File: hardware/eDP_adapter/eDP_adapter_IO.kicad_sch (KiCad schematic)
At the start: 15 parts, among them J1 DF12NB(3.0)-30DS-0.5V(51), J2 DF12NB(3.0)-30DS-0.5V(51), J3 Conn_01x30, J5 Conn_01x06_Socket

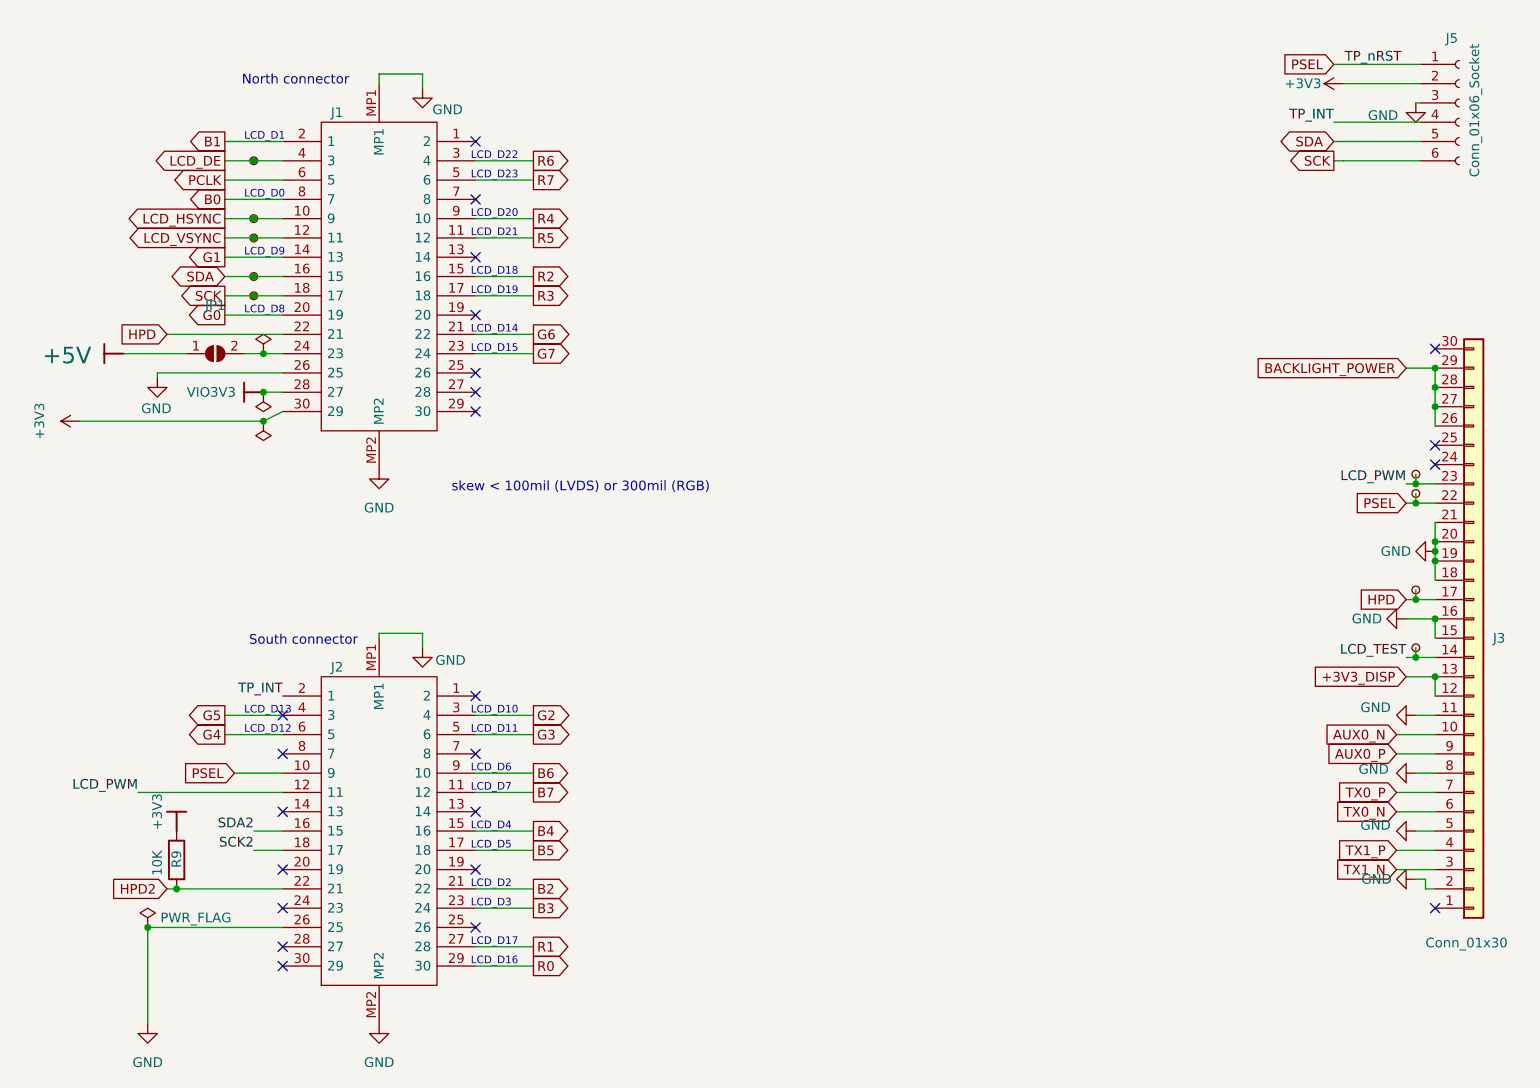
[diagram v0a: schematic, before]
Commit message: change eDP adapter for dual channel LVDS input mode
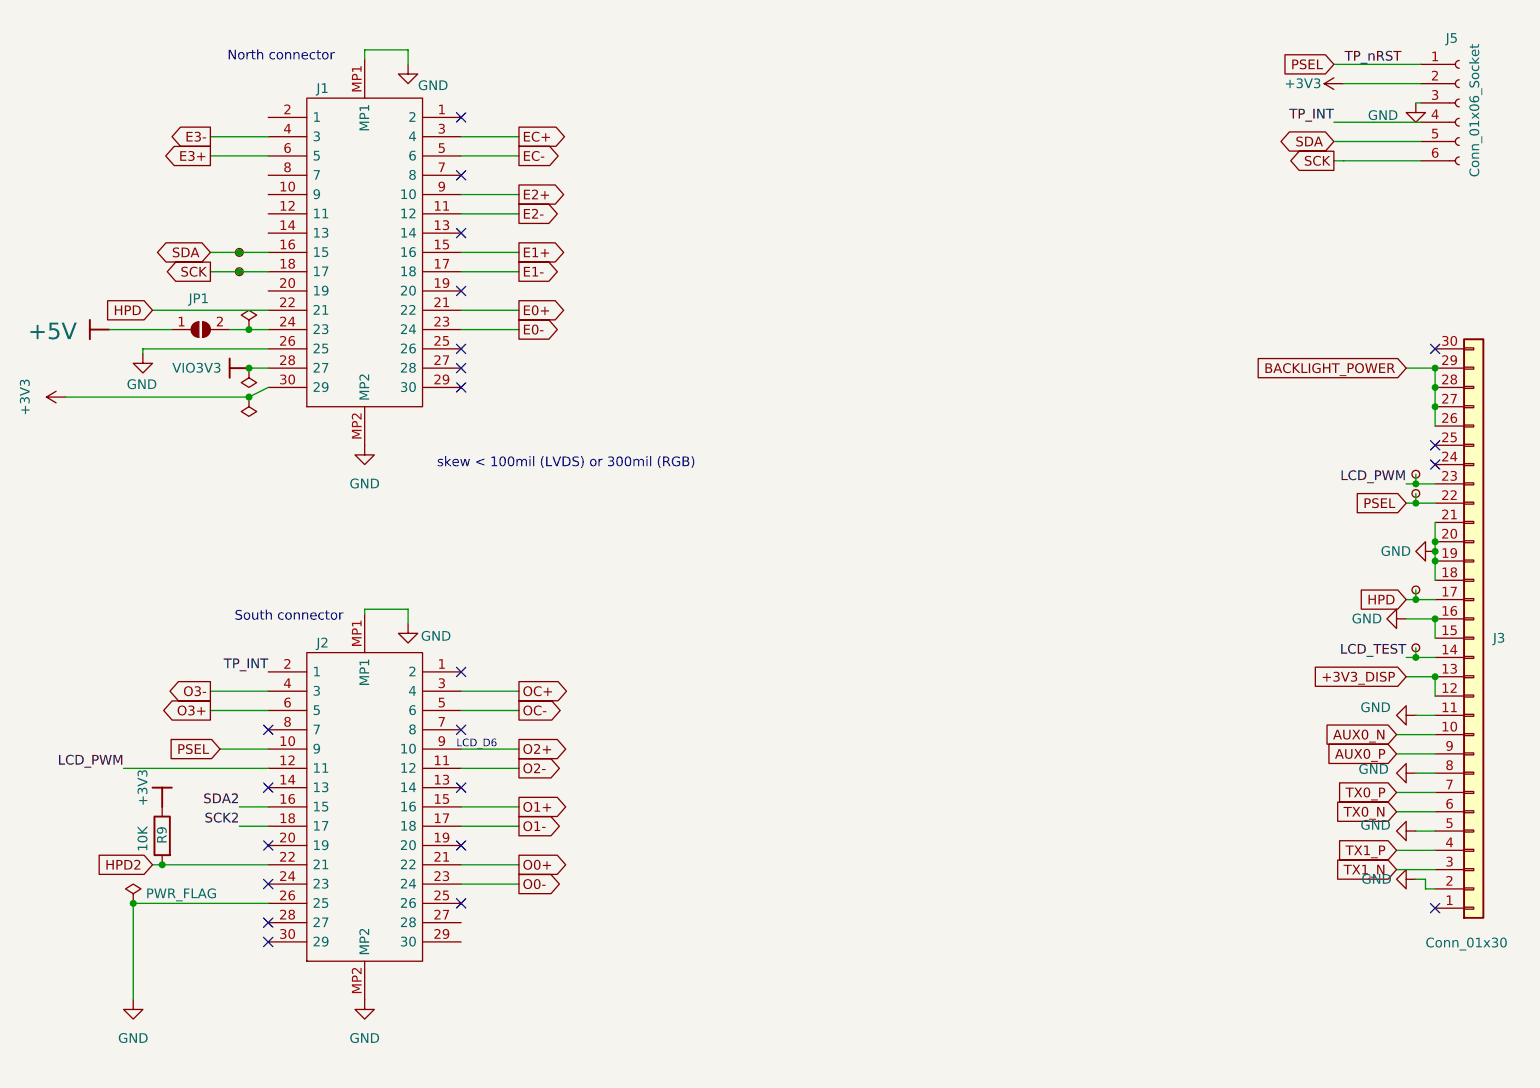
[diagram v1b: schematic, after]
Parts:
- removed TP10, TP11, TP12, TP13, TP14: TestPoint_Small, TestPoint:TestPoint_Pad_D1.0mm, symbol Connector:TestPoint_Small
- added TP1, TP2: TestPoint_Small, TestPoint:TestPoint_Pad_D1.0mm, symbol Connector:TestPoint_Small
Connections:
- net SCK: now also TP2.1
- net SDA: now also TP1.1
- net B0: no longer names the net of J1.8 (7)
- net B1: no longer names the net of J1.2 (1)
- net B2 renamed O0+
- net B3 renamed O0-
- net B4 renamed O1+
- net B5 renamed O1-
- net B6 renamed O2+
- net B7 renamed O2-
- net G0: no longer names the net of J1.20 (19)
- net G1: no longer names the net of J1.14 (13)
- net G2 renamed OC+
- net G3 renamed OC-
- net G4 renamed O3+
- net G5 renamed O3-
- net G6 renamed E0+
- net G7 renamed E0-
- net LCD_DE renamed E3-
- net LCD_HSYNC: no longer names the net of J1.10 (9)
- net LCD_VSYNC: no longer names the net of J1.12 (11)
- net PCLK renamed E3+
- net R0: no longer names the net of J2.29 (30)
- net R1: no longer names the net of J2.27 (28)
- net R2 renamed E1+
- net R3 renamed E1-
- net R4 renamed E2+
- net R5 renamed E2-
- net R6 renamed EC+
- net R7 renamed EC-
- no-connect marks 23 -> 22
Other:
- note removed: "LCD_D0"
- note removed: "LCD_D1"
- note removed: "LCD_D10"
- note removed: "LCD_D11"
- note removed: "LCD_D12"
- note removed: "LCD_D13"
- note removed: "LCD_D14"
- note removed: "LCD_D15"
- note removed: "LCD_D16"
- note removed: "LCD_D17"
- note removed: "LCD_D18"
- note removed: "LCD_D19"
- note removed: "LCD_D2"
- note removed: "LCD_D20"
- note removed: "LCD_D21"
- note removed: "LCD_D22"
- note removed: "LCD_D23"
- note removed: "LCD_D3"
- note removed: "LCD_D4"
- note removed: "LCD_D5"
- note removed: "LCD_D7"
- note removed: "LCD_D8"
- note removed: "LCD_D9"
